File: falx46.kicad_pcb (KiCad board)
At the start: 2 copper layers, 124 parts, among them J1 USB_C_Receptacle_USB2.0, J2 OLED_I2C, J3 AVR-ISP-6, J4 TRRS_I2C, SW1 SW_PUSH, SW10 SW_PUSH, SW11 SW_PUSH, SW12 SW_PUSH, SW13 SW_PUSH, SW14 SW_PUSH, SW15 SW_PUSH, SW16 SW_PUSH, SW17 SW_PUSH, SW18 SW_PUSH, SW19 Rotary_Encoder_Switch, SW2 SW_PUSH, SW20 SW_PUSH, SW21 SW_PUSH, SW22 SW_PUSH, SW23 SW_PUSH, SW24 SW_PUSH, SW25 SW_PUSH, SW26 SW_PUSH, SW27 SW_PUSH, SW28 SW_PUSH, SW29 SW_PUSH, SW3 SW_PUSH, SW30 SW_PUSH, SW31 SW_PUSH, SW32 SW_PUSH, SW33 SW_PUSH, SW34 SW_PUSH, SW35 SW_PUSH, SW36 Rotary_Encoder_Switch, SW37 SW_PUSH, SW38 SW_PUSH, SW39 SW_PUSH, SW4 SW_PUSH, SW40 SW_PUSH, SW41 SW_PUSH, SW42 SW_PUSH, SW43 SW_PUSH, SW44 SW_PUSH, SW45 SW_PUSH, SW46 SW_PUSH, SW47 SW_Push, SW5 SW_PUSH, SW6 SW_PUSH, SW7 SW_PUSH, SW8 SW_PUSH, SW9 SW_PUSH, U1 ATmega32U4-AU, Y1 16MHz

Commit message: 回路図を更新
- Grove I2C端子用ホールを追加
- LEDテープ用接点を追加
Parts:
- added J5: GLOVE_I2C, 1m38_kbd:Grove_I2C, F.Cu at (48.5, 325.9)
- added J6: TRRS_I2C, 1m38_kbd:MJ-4PP-9_1side_backside-mask, F.Cu at (219.6, 315.1)
- C1, C2, C3, C4: footprint Capacitor_SMD:C_0603_1608Metric_Pad1.05x0.95mm_HandSolder -> Capacitor_SMD:C_0805_2012Metric_Pad1.15x1.40mm_HandSolder
- J3: value AVR-ISP-6 -> Conn_LED; footprint 1m38_kbd:ICSP-Header-ZigZag-Single -> foostan-kbd:StripLED_1side; moved to B.Cu
- J4: value TRRS_I2C -> AVR-ISP-6; footprint foostan-kbd:MJ-4PP-9_1side -> 1m38_kbd:ICSP-Header-ZigZag-Single
- U1: moved to F.Cu
- moved SW26 406.9 mm to (56.5, 405.2), turned to 0 degrees
- moved SW28 388.8 mm to (76.7, 385.0)
- moved SW35 382.9 mm to (56.5, 364.8)
- moved SW39 377.0 mm to (36.3, 394.1), turned to 0 degrees
- moved J1 374.0 mm to (29.0, 405.7), turned to 0 degrees
- moved SW32 373.6 mm to (56.5, 385.0), turned to 0 degrees
- moved SW4 360.3 mm to (117.1, 405.2), turned to 0 degrees
- moved SW27 357.3 mm to (96.9, 364.8), turned to 0 degrees
- moved SW34 356.2 mm to (36.3, 333.5)
- moved SW33 351.1 mm to (76.7, 364.8), turned to 0 degrees
- moved SW10 342.0 mm to (96.9, 405.2), turned to 0 degrees
- moved SW41 336.9 mm to (56.5, 344.6)
- moved SW15 330.4 mm to (137.3, 405.2), turned to 0 degrees
- moved SW9 329.9 mm to (117.1, 385.0), turned to 0 degrees
- moved SW42 319.2 mm to (84.8, 324.4)
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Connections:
- J3 pad 1: MISO -> VBUS
- J3 pad 2: VBUS -> LED
- J3 pad 3: ROWL1 -> GND

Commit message: 輪郭線を追加
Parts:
- J1, U1: moved to B.Cu
- R1, R2, R3, R4, R5, R6: footprint Resistor_SMD:R_0603_1608Metric_Pad1.05x0.95mm_HandSolder -> Resistor_SMD:R_0805_2012Metric_Pad1.15x1.40mm_HandSolder
- moved SW26 406.9 mm to (229.6, 36.9), turned to 10 degrees
- moved SW28 388.8 mm to (276.7, 51.6)
- moved SW35 382.9 mm to (295.8, 65.9)
- moved SW39 377.0 mm to (236.2, 74.5), turned to 10 degrees
- moved SW32 373.6 mm to (232.9, 55.7), turned to 10 degrees
- moved SW4 360.3 mm to (117.9, 44.9), turned to 350 degrees
- moved SW27 357.3 mm to (252.8, 43.3), turned to 6 degrees
- moved SW34 356.2 mm to (276.7, 70.6)
- moved J1 353.1 mm to (32.9, 52.7), turned to 90 degrees
- moved SW33 351.1 mm to (254.8, 62.3), turned to 6 degrees
- moved SW10 342.0 mm to (114.5, 63.7), turned to 350 degrees
- moved SW41 336.9 mm to (276.7, 89.7)
- moved SW15 330.4 mm to (72.8, 81.2), turned to 354 degrees
- moved SW9 329.9 mm to (96.6, 55.7), turned to 350 degrees
- moved SW42 319.2 mm to (295.8, 84.9)
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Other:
- board outline added: 281.1 x 112.1 mm

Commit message: 一部パーツを配置
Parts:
- C1, C2, C3, C4, C5, C6, D1, D10, D11, D12, D13, D14, D15, D16, D17, D18, D19, D2, D20, D21, D22, D23, D24, D25, D26, D27, D28, D29, D3, D30, D31, D32, D33, D34, D35, D36, D37, D38, D39, D4, D40, D41, D42, D43, D44, D45, D46, D5, D6, D7, D8, D9, F1, J4, LED1, LED10, LED11, LED12, LED2, LED3, LED4, LED5, LED6, LED7, LED8, LED9, R1, R2, R3, R4, R5, R6, SW47, Y1: moved to B.Cu
- moved J5 312.7 mm to (288.9, 39.3), turned to 252.5 degrees
- moved D41 271.3 mm to (284.9, 90.6), turned to 90 degrees
- moved D32 269.0 mm to (241.2, 55.2), turned to 100 degrees
- moved D26 266.3 mm to (237.9, 36.5), turned to 100 degrees
- moved D1 263.2 mm to (61.0, 52.5), turned to 90 degrees
- moved LED1 262.8 mm to (59.3, 38.2), turned to 180 degrees
- moved D35 261.7 mm to (304.0, 66.8), turned to 90 degrees
- moved D6 257.2 mm to (41.9, 66.8), turned to 90 degrees
- moved D45 251.2 mm to (232.8, 102.4), turned to 100 degrees
- moved D25 249.9 mm to (219.9, 44.5), turned to 100 degrees
- moved R4 249.0 mm to (39.3, 51.2)
- moved R3 248.8 mm to (39.0, 47.5), turned to 180 degrees
- moved D24 247.2 mm to (201.6, 50.1), turned to 100 degrees
- moved D39 243.9 mm to (244.5, 74.0), turned to 100 degrees
- moved J6 242.1 mm to (305.3, 49.5), turned to 270 degrees
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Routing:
- net Net-(F1-Pad2): track 0.00 -> 25.2 mm
- net GND: track 0.00 -> 21.1 mm
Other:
- rule trace_min: 0.2 -> 0.25
- rule via_min_size: 0.4 -> 0.3

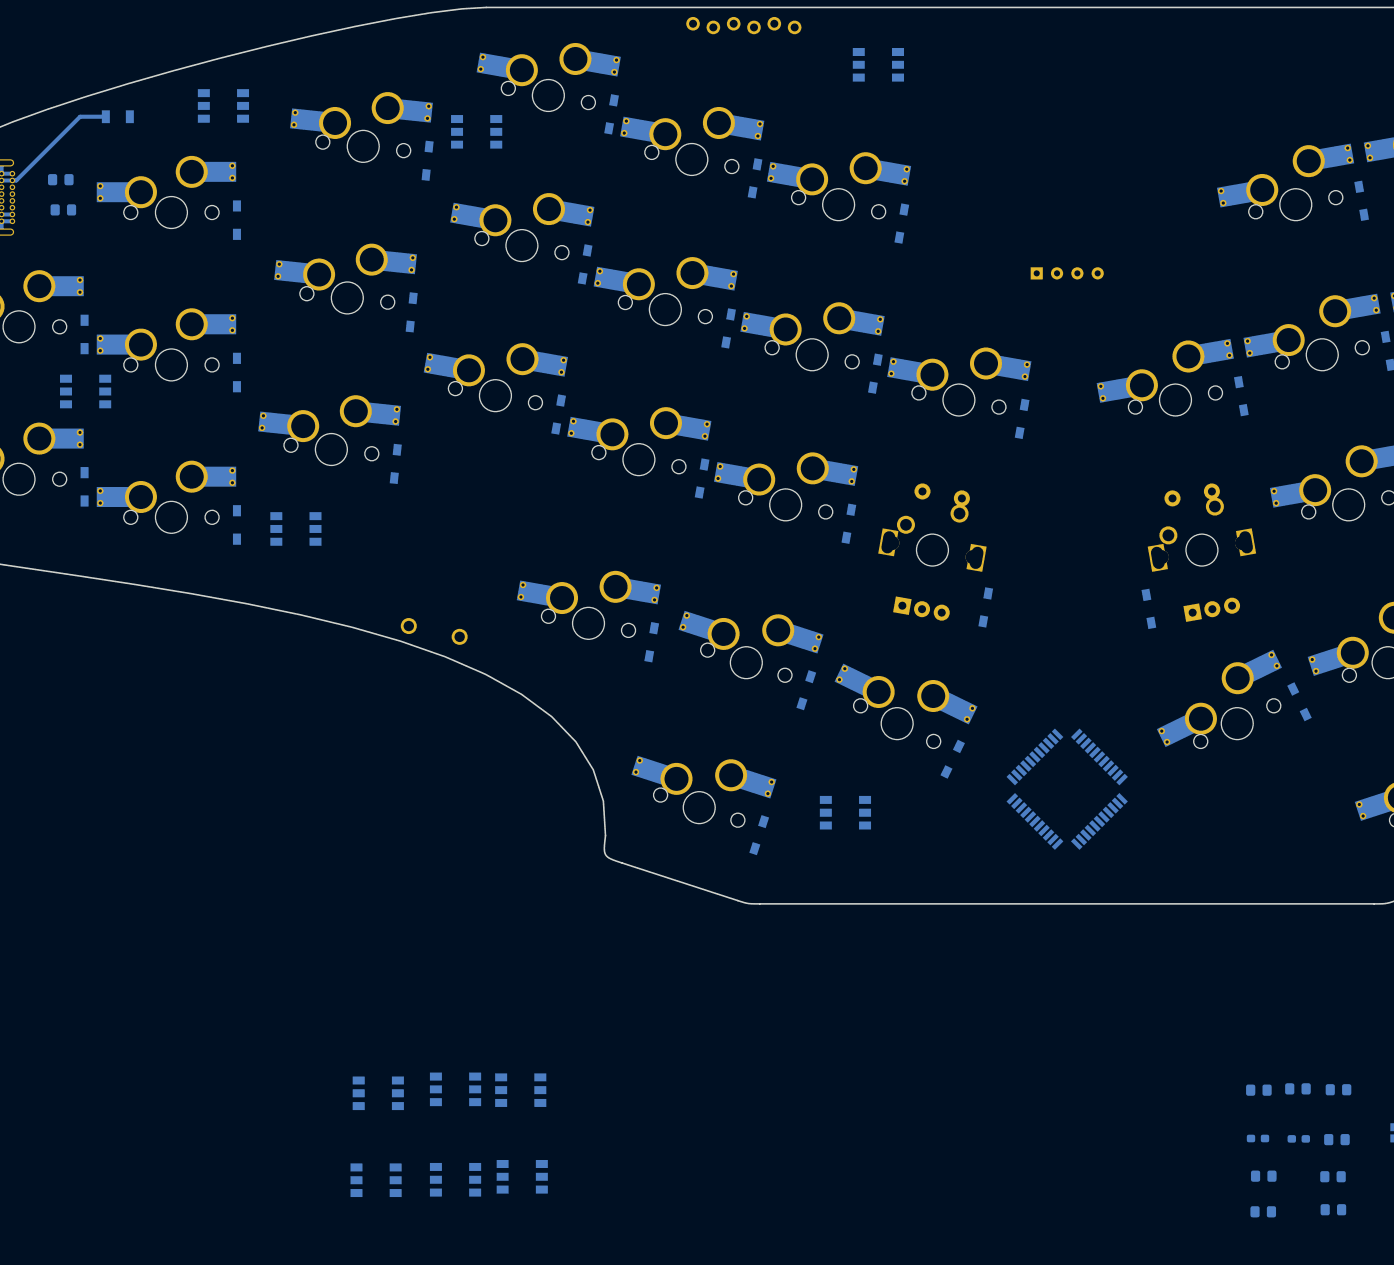
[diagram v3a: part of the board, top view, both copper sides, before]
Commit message: LEDを2つ追加
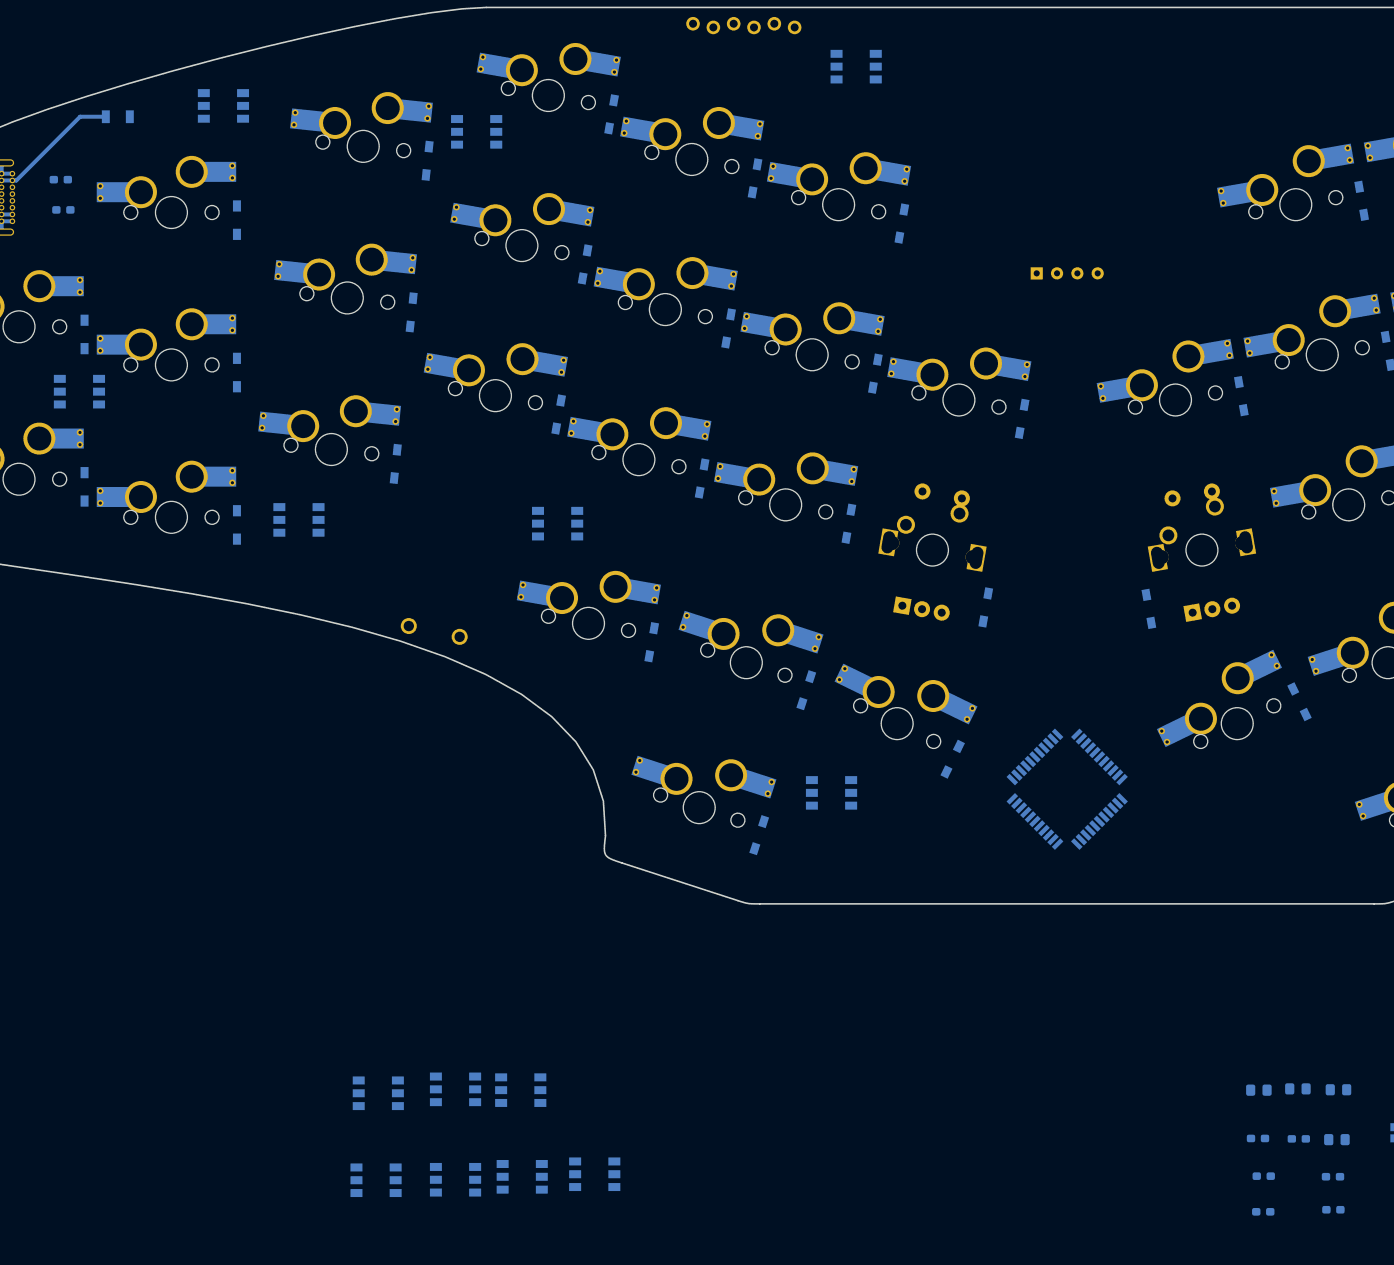
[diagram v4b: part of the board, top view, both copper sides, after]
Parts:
- added LED13: WS2813, LED_SMD:LED_WS2812_PLCC6_5.0x5.0mm_P1.6mm, B.Cu at (68.7, 90.0)
- added LED14: WS2813, LED_SMD:LED_WS2812_PLCC6_5.0x5.0mm_P1.6mm, B.Cu at (41.3, 74.0)
- R1, R2, R3, R4, R5, R6: footprint Resistor_SMD:R_0805_2012Metric_Pad1.15x1.40mm_HandSolder -> Resistor_SMD:R_0603_1608Metric_Pad1.05x0.95mm_HandSolder
- moved LED11 74.6 mm to (135.3, 124.1)
- moved LED12 61.3 mm to (101.1, 90.5)
- moved LED10 55.0 mm to (105.7, 171.8)
- moved LED3 2.79 mm to (138.4, 33.3)

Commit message: オートルータ準備
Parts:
- SW1, SW10, SW11, SW12, SW13, SW14, SW15, SW16, SW17, SW18, SW2, SW20, SW21, SW22, SW23, SW24, SW25, SW26, SW27, SW28, SW29, SW3, SW30, SW31, SW32, SW33, SW34, SW35, SW37, SW38, SW39, SW4, SW40, SW41, SW42, SW43, SW44, SW45, SW46, SW5, SW6, SW7, SW8, SW9: footprint ai03-kbd-MX:MXOnly-1U-Hotswap-Antishear -> 1m38_kbd:CherryMX_Hotswap_mod
- moved LED7 231.9 mm to (288.2, 74.0)
- moved LED6 227.9 mm to (270.2, 38.2)
- moved R2 203.7 mm to (39.4, 48.4)
- moved R1 199.6 mm to (39.4, 51.0)
- moved LED5 192.1 mm to (238.6, 41.5)
- moved LED8 191.2 mm to (260.8, 90.0)
- moved LED4 159.2 mm to (191.2, 33.3)
- moved LED9 155.1 mm to (228.5, 90.5)
- moved R4 143.8 mm to (169.3, 112.6), turned to 270 degrees
- moved R3 143.6 mm to (167.0, 112.6), turned to 90 degrees
- moved R5 125.5 mm to (87.3, 99.0), turned to 341 degrees
- moved LED10 100.5 mm to (194.2, 124.1)
- moved J3 94.5 mm to (76.0, 94.6)
- moved C1 63.8 mm to (160.7, 109.9), turned to 0 degrees
- moved R6 59.1 mm to (149.3, 133.0), turned to 90 degrees
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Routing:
- net VBUS: track 0.00 -> 894.3 mm, vias 0 -> 4
- net GND: track 21.1 -> 896.1 mm, vias 0 -> 4
- net Net-(J1-PadA6): track 0.39 -> 209.3 mm, vias 0 -> 1
- net Net-(J1-PadA7): track 0.15 -> 208.2 mm, vias 0 -> 2
- net COL4: track 0.00 -> 126.7 mm
- net COL5: track 0.00 -> 124.0 mm
- net COL6: track 0.00 -> 105.7 mm
- net COL3: track 0.00 -> 80.5 mm
- net COL2: track 0.00 -> 79.1 mm
- net COL1: track 0.00 -> 76.2 mm
- net COL0: track 0.00 -> 38.1 mm
- net Net-(J1-PadB5): track 0.00 -> 15.7 mm, vias 0 -> 1
- net Net-(D19-Pad2): track 0.00 -> 10.5 mm
- net Net-(D36-Pad2): track 0.00 -> 9.67 mm
- net DP: track 0.21 -> 6.77 mm
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
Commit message: 仮配線
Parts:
- removed the J3 at (76.0, 94.6)
- J1: footprint Connector_USB:USB_C_Receptacle_GCT_USB4085 -> 1m38_kbd:USB_C_Receptacle_GCT_USB4085
- SW1, SW10, SW11, SW12, SW13, SW14, SW15, SW16, SW17, SW18, SW2, SW20, SW21, SW22, SW23, SW24, SW25, SW26, SW27, SW28, SW29, SW3, SW30, SW31, SW32, SW33, SW34, SW35, SW37, SW38, SW39, SW4, SW40, SW41, SW42, SW43, SW44, SW45, SW46, SW5, SW6, SW7, SW8, SW9: footprint 1m38_kbd:CherryMX_Hotswap_mod -> 1m38_kbd:MXOnly-1U-Hotswap-Antishear-mod
- moved SW47 106.0 mm to (186.6, 136.2), turned to 180 degrees
- moved R5 104.5 mm to (186.6, 131.7), turned to 0 degrees
- moved C4 27.5 mm to (167.0, 110.2), turned to 90 degrees
- moved C3 24.8 mm to (164.3, 110.2), turned to 90 degrees
- moved LED13 22.4 mm to (224.3, 112.4)
- moved LED2 22.4 mm to (105.3, 112.4)
- moved LED4 18.9 mm to (36.7, 92.3)
- moved LED11 18.9 mm to (292.8, 92.3)
- moved R3 10.6 mm to (164.3, 102.3)
- moved R4 10.5 mm to (167.0, 102.3)
- moved C6 9.02 mm to (172.1, 133.1)
- moved C5 8.93 mm to (172.1, 135.3)
- moved R6 7.17 mm to (156.1, 135.3), turned to 180 degrees
- moved LED3 6.97 mm to (68.0, 96.9)
- moved LED12 6.97 mm to (261.6, 96.9)
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- renumbered J4 to J3, J5 to J4, J6 to J5, LED11 to LED1, LED6 to LED10, LED7 to LED11, LED8 to LED12, LED9 to LED13, LED10 to LED14, LED12 to LED2, LED13 to LED3, LED14 to LED4, LED1 to LED5, LED2 to LED6, LED3 to LED7, LED4 to LED8, LED5 to LED9
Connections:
- net Net-(J1-PadA6) renamed /DUP
- net Net-(J1-PadA7) renamed /DUN
- D13 pad 1: MOSI -> ROWL2
- D14 pad 1: MOSI -> ROWL2
- D15 pad 1: MOSI -> ROWL2
- D16 pad 1: MOSI -> ROWL2
- D17 pad 1: MOSI -> ROWL2
- D18 pad 1: MOSI -> ROWL2
- D19 pad 1: MOSI -> ROWL2
- D20 pad 1: MISO -> ROWL3
- D21 pad 1: MISO -> ROWL3
- D22 pad 1: MISO -> ROWL3
- D23 pad 1: MISO -> ROWL3
- J3 pad 3: ROWL1 -> SCK
- J4 pad 1: GND -> SDA
- J4 pad 2: VBUS -> SCL
- J4 pad 3: SCL -> VBUS
- J4 pad 4: SDA -> GND
- LED1 pad 4: Net-(LED10-Pad3) (its old number) -> LED
- LED1 pad 6: Net-(LED10-Pad4) (its old number) -> GND
- LED13 pad 3: Net-(LED10-Pad4) (its old number) -> Net-(LED13-Pad3)
- LED14 pad 3: Net-(LED10-Pad3) (its old number) -> Net-(LED14-Pad3)
- LED14 pad 4: Net-(LED10-Pad4) (its old number) -> Net-(LED13-Pad3)
- LED2 pad 6: Net-(LED10-Pad3) (its old number) -> LED
- LED3 pad 3: Net-(LED13-Pad3) -> Net-(LED3-Pad3)
- LED4 pad 3: Net-(LED14-Pad3) -> Net-(LED4-Pad3)
- LED4 pad 4: Net-(LED13-Pad3) -> Net-(LED3-Pad3)
- LED5 pad 4: LED -> Net-(LED4-Pad3)
- LED5 pad 6: GND -> Net-(LED3-Pad3)
- LED6 pad 6: LED -> Net-(LED4-Pad3)
- U1 pad 1: LED -> Net-(U1-Pad1)
- U1 pad 20: ENCR1 -> Net-(U1-Pad20)
- U1 pad 21: ENCR2 -> Net-(U1-Pad21)
- U1 pad 25: COL6 -> Net-(U1-Pad25)
- U1 pad 26: ROWR2 -> Net-(U1-Pad26)
- U1 pad 27: ROWR1 -> Net-(U1-Pad27)
- U1 pad 28: ROWR0 -> Net-(U1-Pad28)
- U1 pad 29: COL6 -> Net-(U1-Pad29)
- U1 pad 30: COL5 -> Net-(U1-Pad30)
- U1 pad 31: COL4 -> Net-(U1-Pad31)
- U1 pad 32: COL3 -> Net-(U1-Pad32)
- U1 pad 36: COL2 -> Net-(U1-Pad36)
- U1 pad 37: COL1 -> Net-(U1-Pad37)
- U1 pad 38: COL0 -> Net-(U1-Pad38)
- U1 pad 39: ENCL1 -> Net-(U1-Pad39)
- U1 pad 40: ENCL2 -> Net-(U1-Pad40)
- U1 pad 8: ROWL0 -> Net-(U1-Pad8)
- U1 pad 9: ROWL1 -> SCK
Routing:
- net SDA: track 0.00 -> 259.3 mm, vias 0 -> 1
- net SCL: track 0.00 -> 256.6 mm, vias 0 -> 1
- net VBUS: track 894.3 -> 734.5 mm, vias 4 -> 7
- net Net-(LED3-Pad3): track 0.00 -> 133.2 mm, vias 0 -> 4
- net GND: track 896.1 -> 773.0 mm, vias 4 -> 9
- net Net-(LED10-Pad4): track 0.00 -> 117.0 mm, vias 0 -> 2
- net Net-(LED7-Pad3): track 0.00 -> 108.4 mm, vias 0 -> 3
- net Net-(LED4-Pad3): track 0.00 -> 106.9 mm, vias 0 -> 4
- net Net-(LED6-Pad3): track 0.00 -> 106.5 mm, vias 0 -> 6
- net Net-(LED1-Pad3): track 0.00 -> 101.1 mm, vias 0 -> 4
- net Net-(LED10-Pad3): track 0.00 -> 100.4 mm, vias 0 -> 3
- net Net-(LED5-Pad3): track 0.00 -> 97.0 mm, vias 0 -> 4
- net Net-(LED10-Pad6): track 0.00 -> 94.2 mm, vias 0 -> 2
- net Net-(LED2-Pad3): track 0.00 -> 91.1 mm, vias 0 -> 4
- net Net-(LED11-Pad3): track 0.00 -> 85.2 mm, vias 0 -> 3
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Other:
- rule trace_min: 0.25 -> 0.2032
- rule via_min_size: 0.3 -> 0.6

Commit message: 仮配線
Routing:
- net MISO: track 0.00 -> 147.3 mm, vias 0 -> 2
- net ROWR1: track 0.00 -> 145.3 mm
- net RESET: track 25.0 -> 170.2 mm
- net SCK: track 0.00 -> 140.6 mm
- net MOSI: track 0.00 -> 139.0 mm
- net ROWL1: track 0.00 -> 132.9 mm
- net COL3: track 80.3 -> 211.3 mm, vias 0 -> 2
- net ROWL2: track 0.00 -> 130.7 mm
- net ROWR2: track 21.0 -> 138.4 mm
- net ROWR0: track 0.00 -> 110.9 mm, vias 0 -> 2
- net ROWL0: track 0.00 -> 94.4 mm
- net COL6: track 94.9 -> 180.2 mm, vias 0 -> 2
- net ROWL3: track 0.00 -> 64.9 mm, vias 0 -> 2
- net GND: track 773.0 -> 802.7 mm
- net Net-(D34-Pad2): track 0.00 -> 22.9 mm
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
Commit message: 仮配線・Mounting Hole追加
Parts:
- added HOLE1: Val**, foostan-kbd:M2_HOLE_v2, F.Cu at (132.0, 133.1)
- added HOLE10: Val**, foostan-kbd:M2_HOLE_v2, F.Cu at (291.5, 92.0)
- added HOLE11: Val**, foostan-kbd:M2_HOLE_v2, F.Cu at (244.9, 100.6)
- added HOLE12: Val**, foostan-kbd:M2_HOLE_v2, F.Cu at (197.6, 133.1)
- added HOLE13: Val**, foostan-kbd:M2_HOLE_v2, F.Cu at (164.8, 88.2)
- added HOLE2: Val**, foostan-kbd:M2_HOLE_v2, F.Cu at (84.6, 100.6)
- added HOLE3: Val**, foostan-kbd:M2_HOLE_v2, F.Cu at (38.0, 92.0)
- added HOLE4: Val**, foostan-kbd:M2_HOLE_v2, F.Cu at (39.7, 43.7)
- added HOLE5: Val**, foostan-kbd:M2_HOLE_v2, F.Cu at (86.3, 32.1)
- added HOLE6: Val**, foostan-kbd:M2_HOLE_v2, F.Cu at (146.0, 31.8)
- added HOLE7: Val**, foostan-kbd:M2_HOLE_v2, F.Cu at (183.6, 31.8)
- added HOLE8: Val**, foostan-kbd:M2_HOLE_v2, F.Cu at (243.2, 32.1)
- added HOLE9: Val**, foostan-kbd:M2_HOLE_v2, F.Cu at (289.8, 43.7)
- moved LED13 21.5 mm to (220.5, 91.3)
- moved LED2 21.5 mm to (109.1, 91.3)
- moved D34 18.2 mm to (286.5, 71.3)
- moved LED4 17.1 mm to (47.3, 79.0)
- moved LED11 17.1 mm to (282.2, 79.0)
- moved LED10 12.2 mm to (262.7, 49.0)
- moved LED5 12.2 mm to (66.8, 49.0)
- moved LED12 8.64 mm to (257.1, 89.5)
- moved LED3 8.64 mm to (72.5, 89.5)
- moved F1 7.78 mm to (46.1, 39.4)
- moved J4 5.19 mm to (284.0, 37.7), turned to 253.5 degrees
- moved D27 3.92 mm to (263.4, 40.3)
- moved LED7 2.88 mm to (138.2, 38.8)
- moved LED8 2.88 mm to (191.4, 38.8)
- moved LED1 2.71 mm to (135.3, 121.4)
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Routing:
- net VBUS: track 731.9 -> 863.0 mm, vias 7 -> 0
- net GND: track 802.7 -> 915.0 mm, vias 9 -> 11
- net Net-(LED10-Pad4): track 117.0 -> 64.1 mm, vias 2 -> 4
- net Net-(LED10-Pad3): track 100.4 -> 67.1 mm
- net Net-(LED4-Pad3): track 106.9 -> 80.1 mm, vias 4 -> 5
- net LED: track 54.2 -> 78.7 mm
- net Net-(LED5-Pad3): track 97.0 -> 73.7 mm
- net (no net): track 17.8 -> 0.00 mm
- net Net-(D34-Pad2): track 22.9 -> 5.56 mm
- net Net-(LED10-Pad6): track 94.2 -> 78.5 mm
- net Net-(LED3-Pad3): track 115.7 -> 101.7 mm, vias 5 -> 3
- net /DUP: track 226.2 -> 239.4 mm, vias 1 -> 3
- net MISO: track 147.3 -> 160.0 mm, vias 2 -> 5
- net /DUN: track 224.2 -> 235.9 mm, vias 2 -> 4
- net Net-(LED13-Pad3): track 41.2 -> 50.4 mm
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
